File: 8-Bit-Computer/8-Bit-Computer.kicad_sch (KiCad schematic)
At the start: 293 parts, among them IC1 AT28C64B-15SU-T, IC2 AT28C64B-15SU-T, IC3 AT28C64B-15SU-T, J1 XLR3_Switched, J2 XLR3_Switched, J3 XLR3_Switched, SW1 SW_Push, SW2 SW_DIP_x04, SW3 SW_DIP_x08, SW4 SW_Push, SW5 SW_Push, U1 NA555D, U10 74LS283, U11 74HC245, U12 74HC86, U13 74HC86, U14 74HC245, U15 HM62256BLP, U16 74HC245, U17 74157, U18 74157, U19 74157, U2 AMS1117-5.0, U20 74HC00, U21 74157, U22 HDSP-7403, U23 74LS377, U24 74LS377, U25 74LS377, U26 74HC245, U27 74LS161, U28 74HC245, U29 74LS377, U3 74HC00, U30 HDSP-7403, U31 74LS377, U32 HDSP-7403, U33 HDSP-7403, U34 74LS107, U35 NA555D, U36 74LS139, U37 74LS161, U38 74LS138, U39 74LS08, U4 LM555xM, U40 74LS04, U41 74LS04, U42 74LS377, U43 74LS00, U44 74HC00, U5 NA555D, U6 74HC00, U7 74HC245, U8 74LS02, U9 74LS283

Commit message: Finished adding footprints
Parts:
- removed J1, J2, J3: XLR3_Switched, symbol Connector_Audio:XLR3_Switched
- removed U4: LM555xM, Package_SO:SOIC-8_3.9x4.9mm_P1.27mm, symbol Timer:LM555xM
- added SW6, SW7, SW8: SW_Push_DPDT, Button_Switch_THT:SW_Tactile_SKHH_Angled, symbol Switch:SW_Push_DPDT
- added U4: NA555D, Package_SO:SOP-8_3.9x4.9mm_P1.27mm, symbol Timer:NA555D
- C1: footprint (none) -> Capacitor_SMD:C_0603_1608Metric
- C10, C11, C12, C13, C14, C15, C16, C17, C18, C19, C20, C21, C22, C23, C24, C25, C26, C27, C28, C29, C3, C30, C31, C32, C33, C34, C35, C36, C37, C38, C39, C40, C41, C42, C5, C6, C7, C9: footprint (none) -> Capacitor_SMD:C_0402_1005Metric
- C2: footprint (none) -> Capacitor_SMD:C_0805_2012Metric
- C4: value C_Polarized -> 1 uF; footprint (none) -> Capacitor_SMD:C_0402_1005Metric
- C8: value C_Small -> 0.01uF; footprint (none) -> Capacitor_SMD:C_0402_1005Metric
- D1, D10, D11, D12, D13, D14, D15, D16, D17, D18, D19, D2, D20, D21, D22, D23, D24, D25, D26, D27, D28, D29, D3, D30, D31, D32, D33, D34, D35, D36, D37, D38, D39, D4, D40, D41, D42, D43, D44, D45, D46, D47, D48, D49, D5, D50, D51, D52, D53, D54, D55, D56, D57, D58, D59, D6, D60, D61, D62, D63, D64, D65, D66, D67, D68, D69, D7, D70, D71, D72, D73, D74, D75, D76, D77, D78, D79, D8, D80, D81, D82, D9: footprint (none) -> LED_SMD:LED_0805_2012Metric
- IC1, IC2, IC3: footprint SOIC127P1032X265-28N -> Package_DIP:DIP-28_W15.24mm_Socket
- R1, R10, R100, R101, R102, R103, R104, R105, R106, R107, R108, R109, R11, R110, R111, R112, R113, R12, R13, R14, R15, R16, R17, R18, R19, R2, R20, R21, R22, R23, R24, R25, R26, R27, R28, R29, R3, R30, R31, R32, R33, R34, R35, R36, R37, R38, R39, R4, R40, R41, R42, R43, R44, R45, R46, R47, R48, R49, R5, R50, R51, R52, R53, R54, R55, R56, R57, R58, R59, R6, R60, R61, R62, R63, R64, R65, R66, R67, R68, R69, R7, R70, R71, R72, R73, R74, R75, R76, R77, R78, R79, R8, R80, R81, R82, R83, R84, R85, R86, R87, R88, R89, R9, R90, R91, R92, R93, R94, R95, R96, R97, R98, R99: footprint (none) -> Resistor_SMD:R_0402_1005Metric
- RV1: footprint (none) -> Potentiometer_SMD:Potentiometer_Bourns_3314G_Vertical
- SW1, SW4, SW5: footprint (none) -> Button_Switch_THT:SW_PUSH_6mm
- SW2: footprint (none) -> Button_Switch_SMD:SW_DIP_SPSTx04_Slide_KingTek_DSHP04TJ_W5.25mm_P1.27mm_JPin
- SW3: footprint (none) -> Button_Switch_SMD:SW_DIP_SPSTx08_Slide_KingTek_DSHP08TJ_W5.25mm_P1.27mm_JPin
- U1, U35, U5: footprint Package_SO:SOIC-8_3.9x4.9mm_P1.27mm -> Package_SO:SOP-8_3.9x4.9mm_P1.27mm
- U10, U9: footprint (none) -> Package_DIP:DIP-16_W7.62mm_Socket
- U11, U14, U16, U26, U28, U7: footprint (none) -> Package_SO:SOIC-20W_7.5x12.8mm_P1.27mm
- U12, U13, U20, U3, U34, U39, U40, U41, U43, U44, U6, U8: footprint (none) -> Package_SO:SOIC-14_3.9x8.7mm_P1.27mm
- U17, U18, U19, U21, U27, U36, U37, U38: footprint (none) -> Package_SO:SOIC-16_3.9x9.9mm_P1.27mm
- U23, U24, U25, U29, U31, U42: footprint (none) -> Package_SO:TSSOP-20_4.4x6.5mm_P0.65mm
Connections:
- net clock_pulse is gone; now on net CLK: C8.1
- net control_logic is gone; now on net RI: U20.2
- net +5V: now also SW6.4 (A), U4.4 (R), U4.8 (VCC)
- net GND: now also SW6.6 (C), SW7.2 (B), SW8.2 (B), U4.1 (GND)
- net PROG: now also SW7.3 (C)
- net RI: no longer U14.19 (CE)
- net WRAM: now also U14.19 (CE)
- net at R5.2, U5.2 (TR): now also SW8.1 (A)
- net at R6.2, U5.4 (R): now also SW8.3 (C)
- net at R3.2, SW1.2: now also U4.2 (TR)
- net at C6.1: now also U4.5 (CV)
- net at U3.5: now also U4.3 (Q)
- net at C5.1, R4.1: now also U4.6 (THR), U4.7 (DIS)
- net at D1.1 (K): now also SW7.1 (A)
- net at IC1.21 (A10): now also SW6.5 (B)

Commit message: finished the PCB layout for ALU and clock
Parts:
- removed U44: 74HC00, Package_SO:SOIC-14_3.9x8.7mm_P1.27mm, symbol 74xx:74HC00
- SW6, SW7, SW8: footprint Button_Switch_THT:SW_Tactile_SKHH_Angled -> Button_Switch_THT:SW_Push_2P2T_Toggle_CK_PVA2xxH4xxxxxxV2
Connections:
- net RI: now also U20.4, U20.5
- net at C4.1, R1.1, U1.2 (TR)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: now also RV1.3; no longer RV1.1
- net at U15.27 (~{WE}): now also U20.6
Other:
- moved on the sheet: U20B
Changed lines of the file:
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@@
 	)
 	(junction
+		(at 118.11 54.5945)
+		(diameter 0)
+		(color 0 0 0 0)
+	)
+	(junction
 		(at 472.44 129.286)
 		(diameter 0)
@@
 	(wire
 		(pts
+			(xy 143.256 63.5) (xy 122.174 63.5)
+		)
+		(stroke
+			(width 0)
+			(type default)
+		)
+	)
+	(wire
+		(pts
 			(xy 284.48 304.038) (xy 312.674 304.038)
 		)
@@
 	(wire
 		(pts
-			(xy 118.11 54.61) (xy 132.08 54.61)
+			(xy 118.11 54.61) (xy 104.14 54.61)
 		)
 		(stroke
@@
 	(wire
 		(pts
+			(xy 122.174 63.5) (xy 122.174 54.5945)
+		)
+		(stroke
+			(width 0)
+			(type default)
+		)
+	)
+	(wire
+		(pts
 			(xy 113.03 119.888) (xy 113.03 124.968)
 		)
@@
 	(wire
 		(pts
-			(xy 118.11 54.61) (xy 118.11 48.26)
+			(xy 118.11 54.61) (xy 118.11 54.5945)
 		)
 		(stroke
@@
 	(wire
 		(pts
+			(xy 139.7 54.61) (xy 143.256 54.61)
+		)
+		(stroke
+			(width 0)
+			(type default)
+		)
+	)
+	(wire
+		(pts
 			(xy 227.584 477.52) (xy 227.584 482.092)
 		)
@@
 	(wire
 		(pts
+			(xy 118.11 54.5945) (xy 118.11 48.26)
+		)
+		(stroke
+			(width 0)
+			(type default)
+		)
+	)
+	(wire
+		(pts
 			(xy 64.135 367.665) (xy 64.135 368.935)
 		)
@@
 	(wire
 		(pts
+			(xy 143.256 54.61) (xy 143.256 63.5)
+		)
+		(stroke
+			(width 0)
+			(type default)
+		)
+	)
+	(wire
+		(pts
 			(xy 750.062 91.313) (xy 776.478 91.313)
 		)
@@
 	(wire
 		(pts
+			(xy 122.174 54.5945) (xy 118.11 54.5945)
+		)
+		(stroke
+			(width 0)
+			(type default)
+		)
+	)
+	(wire
+		(pts
 			(xy 121.412 177.292) (xy 121.412 179.832)
 		)
@@
 	)
 	(symbol
-		(lib_id "74xx:74HC00")
-		(at 615.95 43.688 0)
-		(unit 3)
-		(exclude_from_sim no)
-		(in_bom yes)
-		(on_board yes)
-		(dnp no)
-		(fields_autoplaced yes)
-		(property "Reference" "U44"
-			(at 615.9417 34.29 0)
-			(effects
-				(font
-					(size 1.27 1.27)
-				)
-			)
-		)
-		(property "Value" "74HC00"
-			(at 615.9417 36.83 0)
-			(effects
-				(font
-					(size 1.27 1.27)
-				)
-			)
-		)
-		(property "Footprint" "Package_SO:SOIC-14_3.9x8.7mm_P1.27mm"
-			(at 615.95 43.688 0)
-			(effects
-				(font
-					(size 1.27 1.27)
-				)
-				(hide yes)
-			)
-		)
-		(property "Datasheet" "http://www.ti.com/lit/gpn/sn74hc00"
-			(at 615.95 43.688 0)
-			(effects
-				(font
-					(size 1.27 1.27)
-				)
-				(hide yes)
-			)
-		)
-		(property "Description" ""
-			(at 615.95 43.688 0)
-			(effects
-				(font
-					(size 1.27 1.27)
-				)
-				(hide yes)
-			)
-		)
-		(pin "5"
-		)
-		(pin "6"
-		)
-		(pin "3"
-		)
-		(pin "7"
-		)
-		(pin "14"
-		)
-		(pin "1"
-		)
-		(pin "12"
-		)
-		(pin "2"
-		)
-		(pin "8"
-		)
-		(pin "11"
-		)
-		(pin "13"
-		)
-		(pin "4"
-		)
-		(pin "9"
-		)
-		(pin "10"
-		)
-		(instances
-			(project "8-Bit-Computer"
-				(path "/7068cf22-ceca-4c5f-b7d5-56f579bc3b1d"
-					(reference "U44")
-					(unit 3)
-				)
-			)
-		)
-	)
-	(symbol
 		(lib_id "Device:LED")
 		(at 597.916 384.048 90)
@@
 			)
 		)
-		(property "Footprint" "Button_Switch_THT:SW_Tactile_SKHH_Angled"
+		(property "Footprint" "Button_Switch_THT:SW_Push_2P2T_Toggle_CK_PVA2xxH4xxxxxxV2"
 			(at 588.01 231.394 0)
 			(effects
@@
 			)
 		)
-		(property "Footprint" "Button_Switch_THT:SW_Tactile_SKHH_Angled"
+		(property "Footprint" "Button_Switch_THT:SW_Push_2P2T_Toggle_CK_PVA2xxH4xxxxxxV2"
 			(at 65.913 77.597 0)
 			(effects
@@
 	(symbol
 		(lib_id "74xx:74HC00")
-		(at 795.528 170.688 0)
+		(at 615.95 43.688 0)
 		(unit 2)
 		(exclude_from_sim no)
@@
 		(fields_autoplaced yes)
 		(property "Reference" "U20"
-			(at 795.5197 162.433 0)
+			(at 615.9417 35.433 0)
 			(effects
 				(font
@@
 		)
 		(property "Value" "74HC00"
-			(at 795.5197 164.973 0)
+			(at 615.9417 37.973 0)
 			(effects
 				(font
@@
 		)
 		(property "Footprint" "Package_SO:SOIC-14_3.9x8.7mm_P1.27mm"
-			(at 795.528 170.688 0)
+			(at 615.95 43.688 0)
 			(effects
 				(font
@@
 		)
 		(property "Datasheet" "http://www.ti.com/lit/gpn/sn74hc00"
-			(at 795.528 170.688 0)
+			(at 615.95 43.688 0)
 			(effects
 				(font
@@
 		)
 		(property "Description" ""
-			(at 795.528 170.688 0)
+			(at 615.95 43.688 0)
 			(effects
 				(font
@@
 			)
 		)
-		(property "Footprint" "Button_Switch_THT:SW_Tactile_SKHH_Angled"
+		(property "Footprint" "Button_Switch_THT:SW_Push_2P2T_Toggle_CK_PVA2xxH4xxxxxxV2"
 			(at 243.332 281.94 0)
 			(effects

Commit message: completed display
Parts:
- removed U22, U30, U32, U33: HDSP-7403, Display_7Segment:HDSP-7401, symbol Display_Character:HDSP-7403
- added D83: B_LED, LED_SMD:LED_0805_2012Metric, symbol Device:LED
- added R114: R_US, Resistor_SMD:R_0402_1005Metric, symbol Device:R_US
- added U22, U30, U32, U44: D1X8K-14BL, Display_7Segment:D1X8K, symbol Display_Character:D1X8K-14BL
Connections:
- net CLK: now also R114.1
- net GND: now also D83.1 (K), U22.5 (DP), U30.5 (DP), U32.5 (DP), U44.5 (DP)
- net LCD_A: now also U22.7 (A), U30.7 (A), U32.7 (A), U44.7 (A)
- net LCD_B: now also U22.6 (B), U30.6 (B), U32.6 (B), U44.6 (B); no longer IC1.15 (I/O3)
- net LCD_C: now also U22.4 (C), U30.4 (C), U32.4 (C), U44.4 (C)
- net LCD_E: now also U22.1 (E), U30.1 (E), U32.1 (E), U44.1 (E)
- net LCD_F: now also U22.9 (F), U30.9 (F), U32.9 (F), U44.9 (F)
- net LCD_G: now also U22.10 (G), U30.10 (G), U32.10 (G), U44.10 (G)
- net at U36.4 (O0): now also U44.3 (CC), U44.8 (CC)
- net at U36.5 (O1): now also U22.3 (CC), U22.8 (CC)
- net at U36.6 (O2): now also U30.3 (CC), U30.8 (CC)
- net at U36.7 (O3): now also U32.3 (CC), U32.8 (CC)
- new net: D83.2 (A), R114.2
- new net LCD_D: IC1.15 (I/O3), U22.2 (D), U30.2 (D), U32.2 (D), U44.2 (D)
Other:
- moved on the sheet: U20D

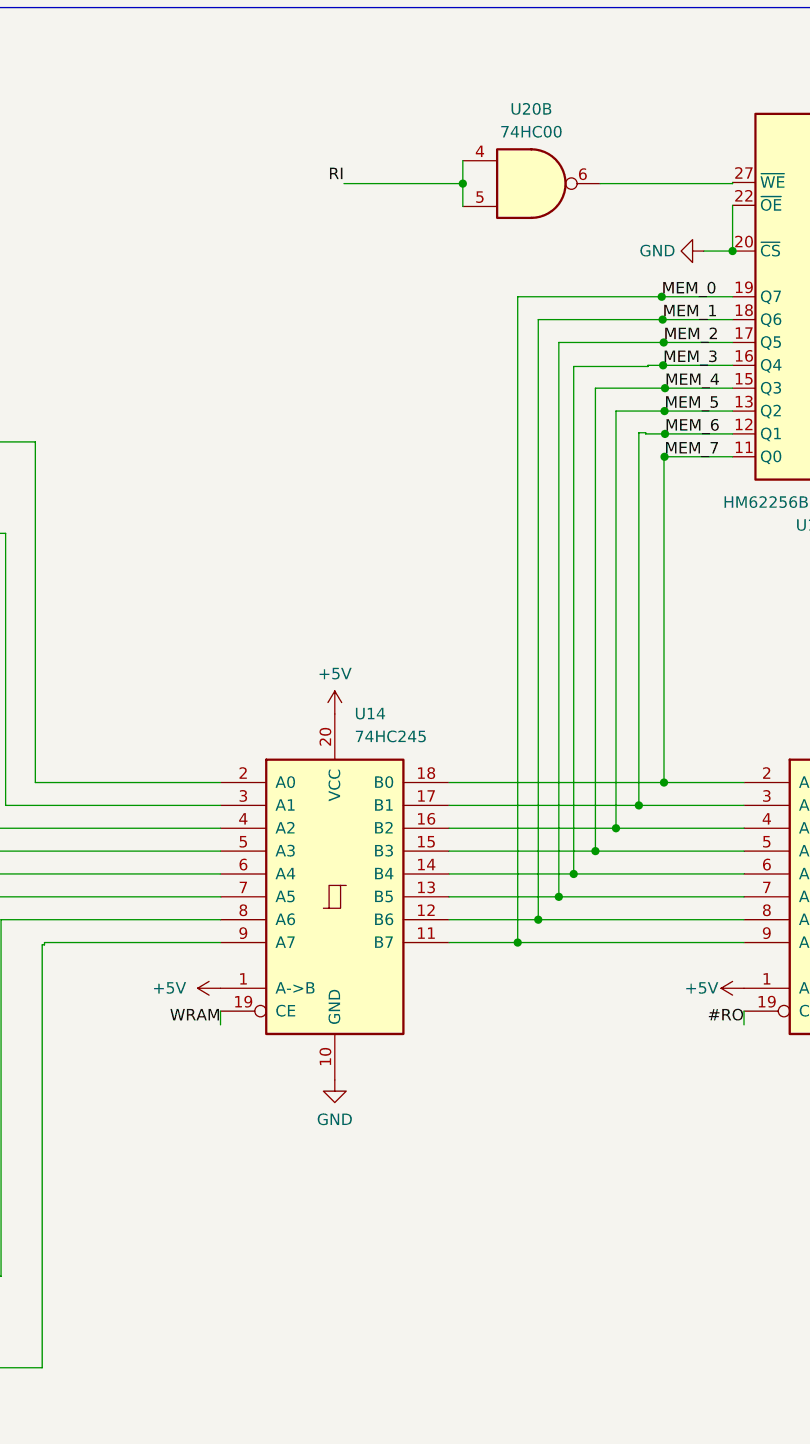
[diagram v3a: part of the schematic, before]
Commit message: Finished Ram and started control logic
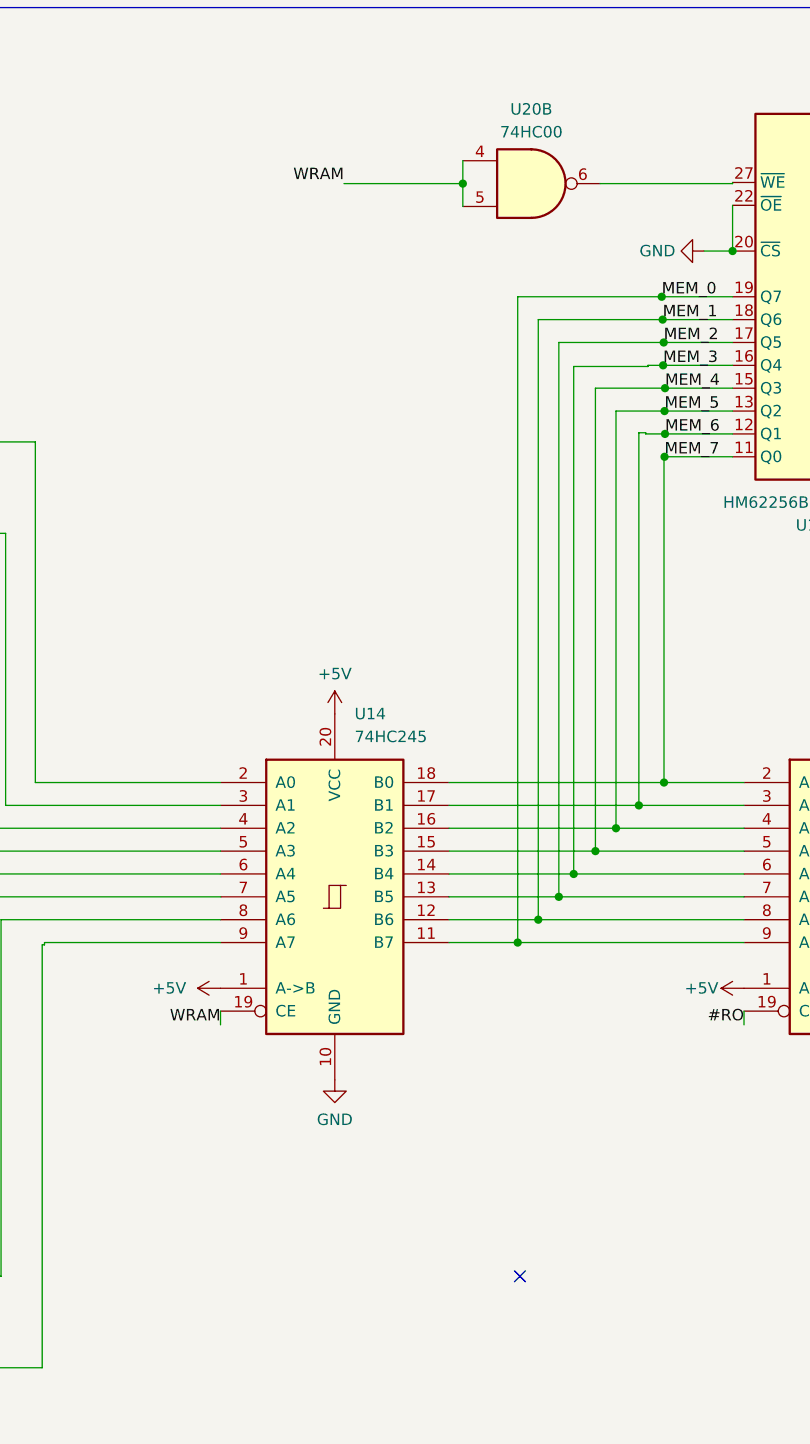
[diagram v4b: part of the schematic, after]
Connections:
- net RI: no longer U20.4, U20.5
- net WRAM: now also U20.4, U20.5
- no-connect marks 2 -> 3
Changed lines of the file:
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@@
 	)
 	(no_connect
+		(at 614.68 165.1)
+	)
+	(no_connect
 		(at 359.41 139.7)
 	)
@@
 		)
 	)
-	(label "RI"
+	(label "WRAM"
 		(at 595.122 43.688 180)
 		(fields_autoplaced yes)

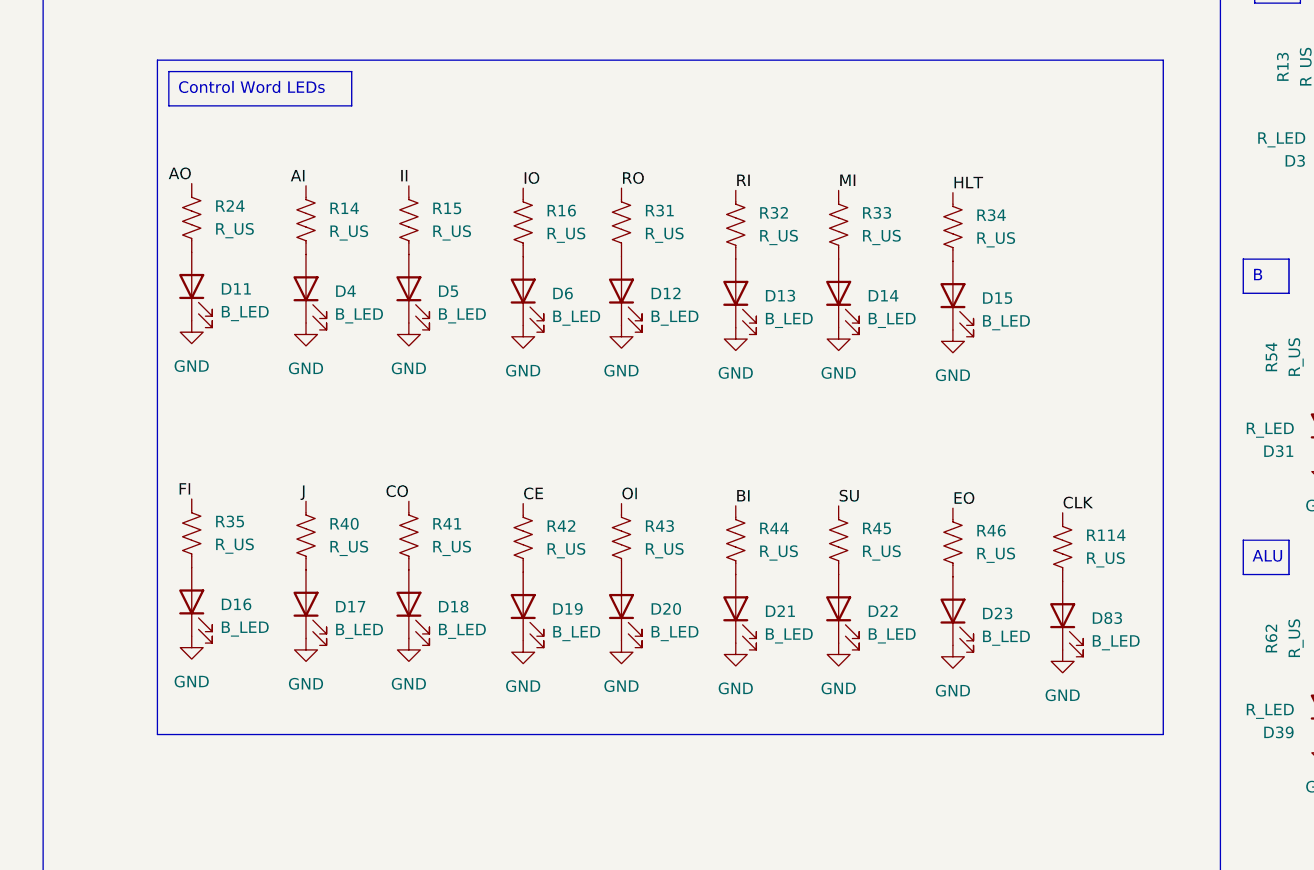
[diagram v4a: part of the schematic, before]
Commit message: removed control word LEDs
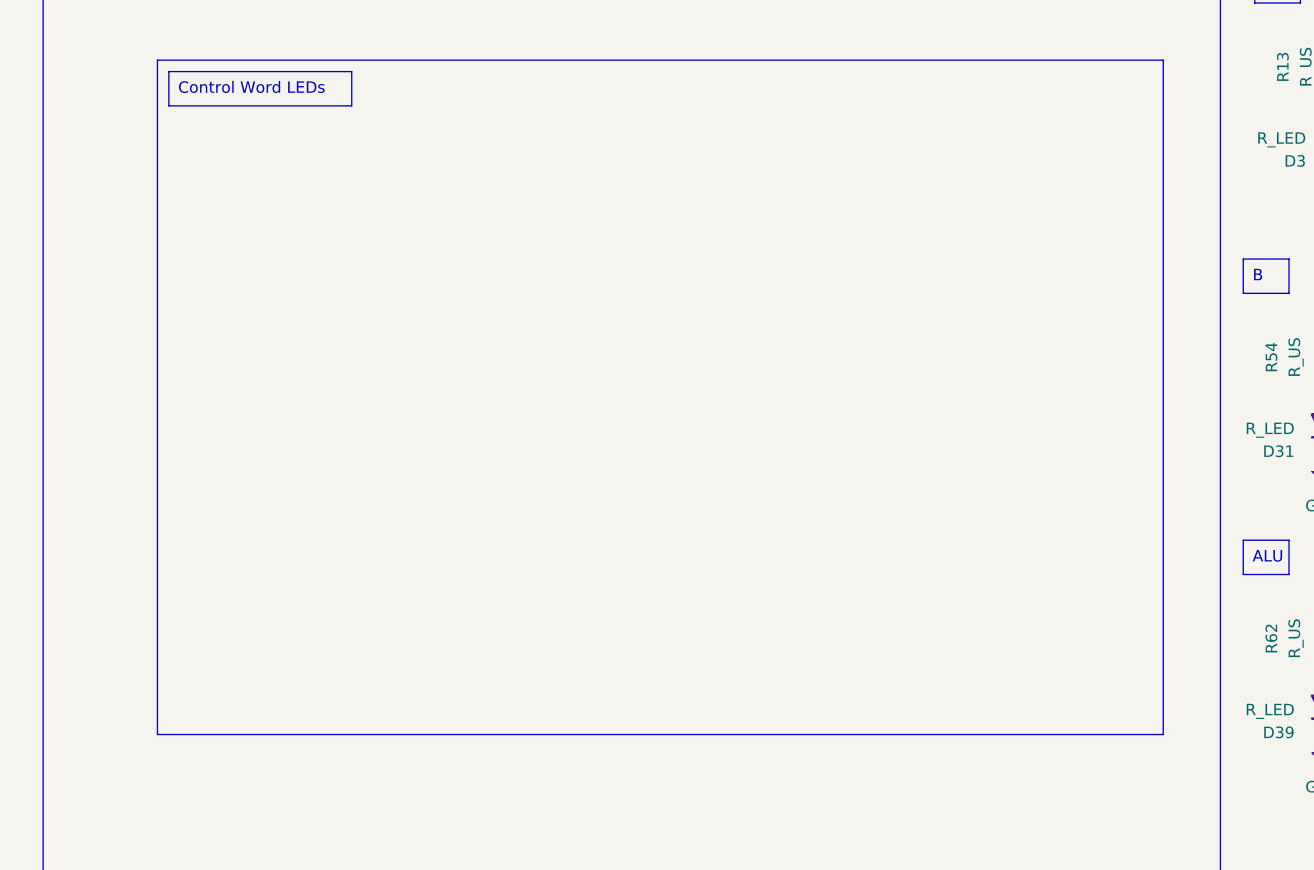
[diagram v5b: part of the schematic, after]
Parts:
- removed D11, D12, D13, D14, D15, D16, D17, D18, D19, D20, D21, D22, D23, D4, D5, D6, D83: B_LED, LED_SMD:LED_0805_2012Metric, symbol Device:LED
- removed R114, R14, R15, R16, R24, R31, R32, R33, R34, R35, R40, R41, R42, R43, R44, R45, R46: R_US, Resistor_SMD:R_0402_1005Metric, symbol Device:R_US

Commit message: Created Gerber Files
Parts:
- added J1: Conn_01x02_Pin, Connector_PinSocket_2.54mm:PinSocket_1x02_P2.54mm_Vertical, symbol Connector:Conn_01x02_Pin
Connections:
- net +9V: now also J1.1 (Pin_1)
- net GND: now also J1.2 (Pin_2)
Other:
- moved on the sheet: C1, C2, U2

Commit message: added R and C values
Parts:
- C11, C12, C13, C14, C15, C16, C17, C18, C19, C20, C21, C22, C23, C24, C25, C26, C27, C28, C29, C30, C31, C32, C33, C34, C35, C36, C37, C38, C39, C40, C41, C42: value C -> 0.1 miF
- C6: value 01 miF -> 0.1 miF
- R100, R101, R102, R103, R104, R105, R106, R107, R108, R109, R110, R111, R112, R113, R13, R27, R28, R29, R30, R47, R48, R49, R50, R51, R52, R53, R54, R55, R56, R57, R58, R59, R60, R61, R62, R63, R64, R65, R66, R67, R68, R69, R70, R71, R72, R73, R74, R75, R76, R77, R86, R87, R88, R89, R90, R91, R92, R93, R94, R95, R96, R97, R98, R99: value R_US -> 220 Ohms
- R12, R5, R7: value R_US -> 1 kOhm
- R78, R79, R80, R81, R82, R83, R84, R85: value R_US -> 10 kOhms
